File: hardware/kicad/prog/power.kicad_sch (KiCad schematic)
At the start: 17 parts, among them J1 AES PROG, J2 Câble PROG-CHA, U1 AMS1117-3.3, U2 AP2112K-1.2

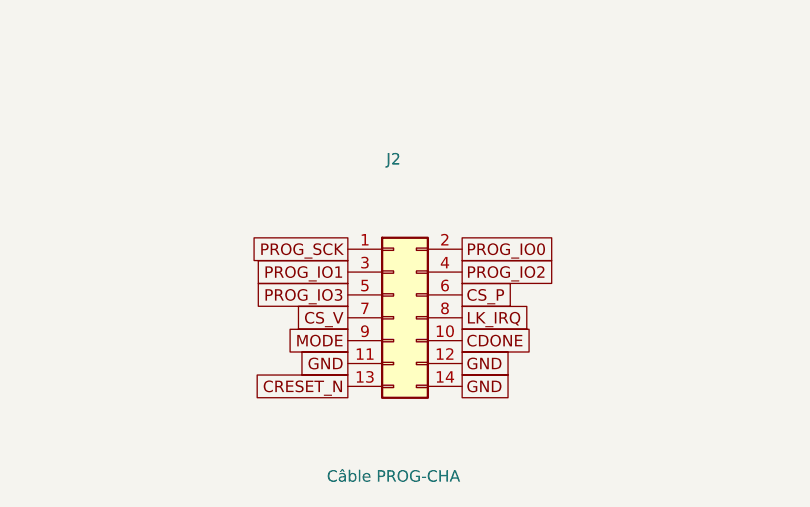
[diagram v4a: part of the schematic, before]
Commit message: Pico 2, microSD et bouton sur la carte PROG ; pistes d'alimentation larges
- La carte PROG est côté avant de la cartouche, composants vers l'avant :
  lecteur microSD et bouton accessibles. Le câble PROG-CHA porte
  désormais le bus de liaison C/SM ; connecteur au même endroit sur les
  deux cartes (x = 172 mm), prêt pour un connecteur carte à carte.
- Sous le Pico : ni piste ni via sur la face composants (pastilles de
  test nues sous le module).
- Classes de réseaux écrites dans le .kicad_pro : +5V et VSYS en 0,5 mm,
  +1V2 en 0,3 mm.
- Broches des FPGA réoptimisées ; contrôle Freerouting sans violation ;
  routage des deux cartes et vérification de timing en cours.

Co-Authored-By: Claude Opus 5.5 <noreply@anthropic.com>
Claude-Session: https://claude.ai/code/session_01WKfXP1YJ8otGxZ5dsY6Agh
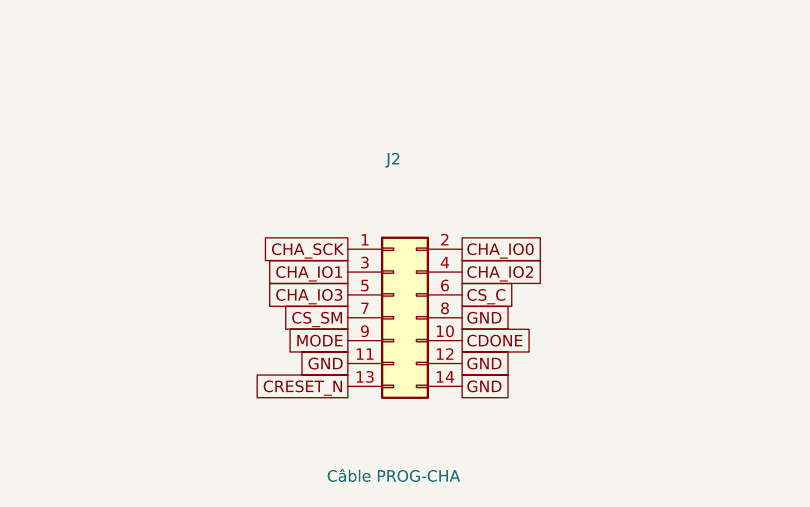
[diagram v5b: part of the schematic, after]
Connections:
- net LK_IRQ is gone; now on net GND: J2.8 (Pin_8)
- net CS_P renamed CS_C
- net CS_V renamed CS_SM
- net PROG_IO0 renamed CHA_IO0
- net PROG_IO1 renamed CHA_IO1
- net PROG_IO2 renamed CHA_IO2
- net PROG_IO3 renamed CHA_IO3
- net PROG_SCK renamed CHA_SCK
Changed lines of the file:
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@@
     (instances
       (project "prog"
-        (path "/da9dbc37-1614-4aa0-819a-d60fb574ce37/b4bc1408-5d78-4d9a-9393-7853520f79f2"
+        (path "/730f52e2-cd0f-4a48-866b-cc2c9ca510b4/9beab20e-506f-43ae-bd9b-cc41a3113d14"
           (reference "J1")
           (unit 1)))))
@@
     (instances
       (project "prog"
-        (path "/da9dbc37-1614-4aa0-819a-d60fb574ce37/b4bc1408-5d78-4d9a-9393-7853520f79f2"
+        (path "/730f52e2-cd0f-4a48-866b-cc2c9ca510b4/9beab20e-506f-43ae-bd9b-cc41a3113d14"
           (reference "R1")
           (unit 1)))))
@@
     (instances
       (project "prog"
-        (path "/da9dbc37-1614-4aa0-819a-d60fb574ce37/b4bc1408-5d78-4d9a-9393-7853520f79f2"
+        (path "/730f52e2-cd0f-4a48-866b-cc2c9ca510b4/9beab20e-506f-43ae-bd9b-cc41a3113d14"
           (reference "R2")
           (unit 1)))))
@@
     (instances
       (project "prog"
-        (path "/da9dbc37-1614-4aa0-819a-d60fb574ce37/b4bc1408-5d78-4d9a-9393-7853520f79f2"
+        (path "/730f52e2-cd0f-4a48-866b-cc2c9ca510b4/9beab20e-506f-43ae-bd9b-cc41a3113d14"
           (reference "C1")
           (unit 1)))))
@@
     (instances
       (project "prog"
-        (path "/da9dbc37-1614-4aa0-819a-d60fb574ce37/b4bc1408-5d78-4d9a-9393-7853520f79f2"
+        (path "/730f52e2-cd0f-4a48-866b-cc2c9ca510b4/9beab20e-506f-43ae-bd9b-cc41a3113d14"
           (reference "C2")
           (unit 1)))))
@@
     (instances
       (project "prog"
-        (path "/da9dbc37-1614-4aa0-819a-d60fb574ce37/b4bc1408-5d78-4d9a-9393-7853520f79f2"
+        (path "/730f52e2-cd0f-4a48-866b-cc2c9ca510b4/9beab20e-506f-43ae-bd9b-cc41a3113d14"
           (reference "U1")
           (unit 1)))))
@@
     (instances
       (project "prog"
-        (path "/da9dbc37-1614-4aa0-819a-d60fb574ce37/b4bc1408-5d78-4d9a-9393-7853520f79f2"
+        (path "/730f52e2-cd0f-4a48-866b-cc2c9ca510b4/9beab20e-506f-43ae-bd9b-cc41a3113d14"
           (reference "C3")
           (unit 1)))))
@@
     (instances
       (project "prog"
-        (path "/da9dbc37-1614-4aa0-819a-d60fb574ce37/b4bc1408-5d78-4d9a-9393-7853520f79f2"
+        (path "/730f52e2-cd0f-4a48-866b-cc2c9ca510b4/9beab20e-506f-43ae-bd9b-cc41a3113d14"
           (reference "C4")
           (unit 1)))))
@@
     (instances
       (project "prog"
-        (path "/da9dbc37-1614-4aa0-819a-d60fb574ce37/b4bc1408-5d78-4d9a-9393-7853520f79f2"
+        (path "/730f52e2-cd0f-4a48-866b-cc2c9ca510b4/9beab20e-506f-43ae-bd9b-cc41a3113d14"
           (reference "U2")
           (unit 1)))))
@@
     (instances
       (project "prog"
-        (path "/da9dbc37-1614-4aa0-819a-d60fb574ce37/b4bc1408-5d78-4d9a-9393-7853520f79f2"
+        (path "/730f52e2-cd0f-4a48-866b-cc2c9ca510b4/9beab20e-506f-43ae-bd9b-cc41a3113d14"
           (reference "C5")
           (unit 1)))))
@@
     (instances
       (project "prog"
-        (path "/da9dbc37-1614-4aa0-819a-d60fb574ce37/b4bc1408-5d78-4d9a-9393-7853520f79f2"
+        (path "/730f52e2-cd0f-4a48-866b-cc2c9ca510b4/9beab20e-506f-43ae-bd9b-cc41a3113d14"
           (reference "C6")
           (unit 1)))))
@@
     (instances
       (project "prog"
-        (path "/da9dbc37-1614-4aa0-819a-d60fb574ce37/b4bc1408-5d78-4d9a-9393-7853520f79f2"
+        (path "/730f52e2-cd0f-4a48-866b-cc2c9ca510b4/9beab20e-506f-43ae-bd9b-cc41a3113d14"
           (reference "R3")
           (unit 1)))))
@@
     (instances
       (project "prog"
-        (path "/da9dbc37-1614-4aa0-819a-d60fb574ce37/b4bc1408-5d78-4d9a-9393-7853520f79f2"
+        (path "/730f52e2-cd0f-4a48-866b-cc2c9ca510b4/9beab20e-506f-43ae-bd9b-cc41a3113d14"
           (reference "R4")
           (unit 1)))))
@@
     (instances
       (project "prog"
-        (path "/da9dbc37-1614-4aa0-819a-d60fb574ce37/b4bc1408-5d78-4d9a-9393-7853520f79f2"
+        (path "/730f52e2-cd0f-4a48-866b-cc2c9ca510b4/9beab20e-506f-43ae-bd9b-cc41a3113d14"
           (reference "R5")
           (unit 1)))))
@@
     (instances
       (project "prog"
-        (path "/da9dbc37-1614-4aa0-819a-d60fb574ce37/b4bc1408-5d78-4d9a-9393-7853520f79f2"
+        (path "/730f52e2-cd0f-4a48-866b-cc2c9ca510b4/9beab20e-506f-43ae-bd9b-cc41a3113d14"
           (reference "R6")
           (unit 1)))))
@@
     (instances
       (project "prog"
-        (path "/da9dbc37-1614-4aa0-819a-d60fb574ce37/b4bc1408-5d78-4d9a-9393-7853520f79f2"
+        (path "/730f52e2-cd0f-4a48-866b-cc2c9ca510b4/9beab20e-506f-43ae-bd9b-cc41a3113d14"
           (reference "R7")
           (unit 1)))))
@@
     (instances
       (project "prog"
-        (path "/da9dbc37-1614-4aa0-819a-d60fb574ce37/b4bc1408-5d78-4d9a-9393-7853520f79f2"
+        (path "/730f52e2-cd0f-4a48-866b-cc2c9ca510b4/9beab20e-506f-43ae-bd9b-cc41a3113d14"
           (reference "J2")
           (unit 1)))))
-  (global_label "PROG_SCK"
+  (global_label "CHA_SCK"
     (shape passive)
     (at 274.32 187.96 180)
@@
         (font
           (size 1.27 1.27)) hide)))
-  (global_label "PROG_IO0"
+  (global_label "CHA_IO0"
     (shape passive)
     (at 287.02 187.96 0)
@@
         (font
           (size 1.27 1.27)) hide)))
-  (global_label "PROG_IO1"
+  (global_label "CHA_IO1"
     (shape passive)
     (at 274.32 190.5 180)
@@
         (font
           (size 1.27 1.27)) hide)))
-  (global_label "PROG_IO2"
+  (global_label "CHA_IO2"
     (shape passive)
     (at 287.02 190.5 0)
@@
         (font
           (size 1.27 1.27)) hide)))
-  (global_label "PROG_IO3"
+  (global_label "CHA_IO3"
     (shape passive)
     (at 274.32 193.04 180)
@@
         (font
           (size 1.27 1.27)) hide)))
-  (global_label "CS_P"
+  (global_label "CS_C"
     (shape passive)
     (at 287.02 193.04 0)
@@
         (font
           (size 1.27 1.27)) hide)))
-  (global_label "CS_V"
+  (global_label "CS_SM"
     (shape passive)
     (at 274.32 195.58 180)
@@
         (font
           (size 1.27 1.27)) hide)))
-  (global_label "LK_IRQ"
+  (global_label "GND"
     (shape passive)
     (at 287.02 195.58 0)

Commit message: Régulateur 3,3 V à découpage, horloge SDRAM adaptée côté FPGA, U8 en 74AHCT125
- AP63203 (TSOT-23-6, sortie fixe 3,3 V, ~90 %) à la place de
  l'AMS1117 : ~0,15 W de pertes au lieu de ~0,75 W et moins de courant
  tiré sur le 5 V de la console ; L 4,7 µH, Cin 10 µF, Cout 2 x 22 µF.
- Résistance série de 33 ohms de l'horloge SDRAM déclarée avec le FPGA :
  placée à 2,7 mm de sa broche (au lieu de ~30 mm, côté SDRAM).
- CHA : U8 (16244 pour 2 canaux) remplacé par un 74AHCT125.
Cartes replacées, contrôle Freerouting sans violation ; routage des
deux cartes et vérification de timing en cours.

Co-Authored-By: Claude Opus 5.5 <noreply@anthropic.com>
Claude-Session: https://claude.ai/code/session_01WKfXP1YJ8otGxZ5dsY6Agh
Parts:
- removed U1: AMS1117-3.3, Package_TO_SOT_SMD:SOT-223-3_TabPin2, symbol Regulator_Linear:AMS1117-3.3
- added C7: 10u, Capacitor_SMD:C_0805_2012Metric, symbol Device:C
- added C8: 1u, Capacitor_SMD:C_0603_1608Metric, symbol Device:C
- added L1: 4,7 µH 3 A, Inductor_SMD:L_Bourns_SRP5030T, symbol Device:L
- added U1: AP63203WU, Package_TO_SOT_SMD:TSOT-23-6, symbol Regulator_Switching:AP63203WU
- C1: value 22u -> 10u; footprint Capacitor_SMD:C_1206_3216Metric -> Capacitor_SMD:C_0805_2012Metric
- C5: value 10u -> 22u; footprint Capacitor_SMD:C_0805_2012Metric -> Capacitor_SMD:C_1206_3216Metric
- C6: value 1u -> 22u; footprint Capacitor_SMD:C_0603_1608Metric -> Capacitor_SMD:C_1206_3216Metric
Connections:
- net +1V2: now also C7.1; no longer C5.1
- net +3V3: now also C5.1, C8.1, L1.2, U1.1 (FB); no longer C3.1, C4.1
- net +5V: now also C3.1, U1.2 (EN), U1.3 (IN)
- net GND: now also C7.2, C8.2, U1.4 (GND); no longer C4.2
- new net BST33: C4.1, U1.6 (BST)
- new net SW33: C4.2, L1.1, U1.5 (SW)
